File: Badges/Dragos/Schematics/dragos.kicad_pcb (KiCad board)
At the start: 2 copper layers, 78.5 x 67.3 mm, 28 parts, among them J7 USB_C_Receptacle, SW1 SW_DIP_x01, SW2 Prog, SW3 Power, U1 STM32F042F6Px, U2 TLV1117-33, U3 HX4056

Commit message: Progress on Dragos badge
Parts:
- removed BT1: Battery_Cell, Tests:Dongguan14500
- removed C1, C2: 20pF, Capacitor_SMD:C_0805_2012Metric
- removed C10, C11, C6: 1uF, Capacitor_SMD:C_0805_2012Metric
- removed C3, C5: 100nF, Capacitor_SMD:C_0805_2012Metric
- removed C4: 4.7uF, Capacitor_SMD:C_0805_2012Metric
- removed C7: 10nF, Capacitor_SMD:C_0805_2012Metric
- removed C8, C9: 10uF, Capacitor_SMD:C_0805_2012Metric
- removed the G*** at (135.4, 99.1) (x4)
- removed J7: USB_C_Receptacle, Tests:USB_C_Receptical-Jing
- removed R1, R2, R3: 10k, Resistor_SMD:R_0805_2012Metric
- removed R5: 1.5, Resistor_SMD:R_0805_2012Metric
- removed R6: 1k, Resistor_SMD:R_0805_2012Metric
- removed SW1: SW_DIP_x01, Button_Switch_SMD:SW_Push_1P1T_NO_CK_KSC7xxJ
- removed SW2: Prog, BreadBoardPwr:SK-3296S_switch
- removed SW3: Power, BreadBoardPwr:SK-3296S_switch
- removed U1: STM32F042F6Px, Package_SO:TSSOP-20_4.4x6.5mm_P0.65mm
- removed U2: TLV1117-33, Package_TO_SOT_SMD:SOT-223-3_TabPin2
- removed U3: HX4056, Package_SO:HSOP-8-1EP_3.9x4.9mm_P1.27mm_EP2.41x3.1mm
- added G*** (x6): LOGO, LOGO, F.Cu at (0.00, 0.00)
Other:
- board size 78.5 x 67.3 mm -> 98.7 x 84.6 mm

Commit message: Almost done
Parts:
- removed the G*** at (0.00, 0.00) (x6)
- added BT1: Battery_Cell, Tests:Dongguan14500, B.Cu at (134.5, 64.5)
- added C1: 100nF, Capacitor_SMD:C_0805_2012Metric, B.Cu at (271.2, 105.2)
- added C10: 1uF, Capacitor_SMD:C_0805_2012Metric, B.Cu at (127.9, 76.8)
- added C11: 1uF, Capacitor_SMD:C_0805_2012Metric, B.Cu at (142.3, 78.8)
- added C12: 100nF, Capacitor_SMD:C_0805_2012Metric, B.Cu at (239.5, 99.2)
- added C13: 1uF, Capacitor_SMD:C_0805_2012Metric, B.Cu at (280.0, 108.2)
- added C14: 4.7uF, Capacitor_SMD:C_0805_2012Metric, B.Cu at (235.1, 99.2)
- added C15: 10pF, Capacitor_SMD:C_0805_2012Metric, B.Cu at (248.3, 102.1)
- added C16: 10pF, Capacitor_SMD:C_0805_2012Metric, B.Cu at (239.5, 102.1)
- added C17: 2.2pF, Capacitor_SMD:C_0805_2012Metric, B.Cu at (235.1, 102.1)
- added C18: 2.2pF, Capacitor_SMD:C_0805_2012Metric, B.Cu at (243.9, 102.1)
- added C2: 100nF, Capacitor_SMD:C_0805_2012Metric, B.Cu at (275.6, 105.2)
- added C3: 100nF, Capacitor_SMD:C_0805_2012Metric, B.Cu at (280.0, 105.2)
- added C4: 100nF, Capacitor_SMD:C_0805_2012Metric, B.Cu at (271.2, 102.3)
- added C5: 100nF, Capacitor_SMD:C_0805_2012Metric, B.Cu at (275.6, 102.3)
- added C6: 4.7uF, Capacitor_SMD:C_0805_2012Metric, B.Cu at (279.7, 120.0)
- added C7: 100nF, Capacitor_SMD:C_0805_2012Metric, B.Cu at (280.0, 102.3)
- added C8: 10uF, Capacitor_SMD:C_0805_2012Metric, B.Cu at (113.6, 77.7)
- added C9: 10uF, Capacitor_SMD:C_0805_2012Metric, B.Cu at (127.9, 73.5)
- added D1: LED, LED_SMD:LED_0603_1608Metric, B.Cu at (275.2, 99.5)
- added D2: LED, LED_SMD:LED_0603_1608Metric, B.Cu at (279.3, 99.5)
- added D3: LED_ALT, Dragos:T776-ReverseMountLED, B.Cu at (186.5, 80.3)
- added G*** (x2): LOGO, LOGO, F.Cu at (0.00, 0.00)
- added G*** (x4): LOGO, LOGO, F.Cu at (145.3, 95.3)
- added J1: One, Connector_PinHeader_2.54mm:PinHeader_1x08_P2.54mm_Vertical, B.Cu at (230.5, 112.6)
- added J2: Two, Connector_PinHeader_2.54mm:PinHeader_1x11_P2.54mm_Vertical, B.Cu at (208.2, 112.6)
- added J3: CC2530-ISP, Connector_PinHeader_2.54mm:PinHeader_2x05_P2.54mm_Vertical, B.Cu at (235.2, 95.3)
- added J4: Three, Connector_PinHeader_2.54mm:PinHeader_1x14_P2.54mm_Vertical, B.Cu at (203.6, 112.6)
- added J5: Prog, Connector_PinHeader_2.54mm:PinHeader_1x06_P2.54mm_Vertical, B.Cu at (255.2, 112.6)
- added J6: Oled_FFS, Connector_FFC-FPC:TE_1-84953-0_1x10-1MP_P1.0mm_Horizontal, B.Cu at (242.9, 111.1)
- added J7: USB_C_Receptacle, Tests:USB_C_Receptical-Jing, B.Cu at (177.4, 126.2)
- added J8: Four, Connector_PinHeader_2.54mm:PinHeader_1x13_P2.54mm_Vertical, B.Cu at (266.7, 119.1)
- added J9: BreadboardPwr, Connector_PinHeader_2.54mm:PinHeader_1x02_P2.54mm_Vertical, B.Cu at (259.8, 112.6)
- added L1: L_Small, Inductor_SMD:L_0603_1608Metric, B.Cu at (275.2, 97.0)
- added Power ->: Power, BreadBoardPwr:SK-3296S_switch, B.Cu at (162.6, 85.9)
- added R11: 330Ohm, Resistor_SMD:R_0805_2012Metric, B.Cu at (271.2, 111.1)
- added R12: 330Ohm, Resistor_SMD:R_0805_2012Metric, B.Cu at (275.6, 111.1)
- added R13: 4k7, Resistor_SMD:R_0805_2012Metric, B.Cu at (280.0, 111.1)
- added R14: 4k7, Resistor_SMD:R_0805_2012Metric, B.Cu at (271.2, 108.2)
- added R3: 100k, Resistor_SMD:R_0805_2012Metric, B.Cu at (275.6, 108.2)
- added R5: 1.5, Resistor_SMD:R_0805_2012Metric, B.Cu at (113.6, 74.4)
- added R6: 1k, Resistor_SMD:R_0805_2012Metric, B.Cu at (113.7, 80.9)
- added R9: 1k, Resistor_SMD:R_0805_2012Metric, B.Cu at (279.7, 114.1)
- added RN1: 10k, Resistor_SMD:R_Array_Concave_2x0603, B.Cu at (271.1, 99.2)
- added RN2: 4k7, Resistor_SMD:R_Array_Concave_4x0603, B.Cu at (155.8, 109.9)
- added SW1: SW_DIP_x01, Button_Switch_SMD:SW_Push_1P1T_NO_CK_KSC7xxJ, B.Cu at (161.3, 96.7)
- added SW2: SW_DIP_x01, Dragos:1TS002E-2500-2500-CT-HYP-Button, F.Cu at (178.2, 117.9)
- added SW4: SW_DIP_x01, Dragos:1TS002E-2500-2500-CT-HYP-Button, F.Cu at (183.7, 117.9)
- added U1: STM32F411RETx, Package_QFP:LQFP-64_10x10mm_P0.5mm, B.Cu at (163.8, 126.6)
- added U2: TLV1117-33, Package_TO_SOT_SMD:SOT-223-3_TabPin2, B.Cu at (136.3, 76.6)
- added U3: HX4056, Package_SO:HSOP-8-1EP_3.9x4.9mm_P1.27mm_EP2.41x3.1mm, B.Cu at (120.5, 76.3)
- added U4: EByte-CC2530, RF_Module:E18-MS1-PCB, B.Cu at (140.8, 102.8)
- added U5: K1-5202UA-03(5Way_Switch), Dragos:K1-5202UA-03(5way-switch), F.Cu at (151.6, 116.9)
- added Y1: 12MHz, Crystal:Crystal_SMD_SeikoEpson_TSX3225-4Pin_3.2x2.5mm, B.Cu at (260.1, 105.5)
- added Y2: 32.768kHz, Crystal:Crystal_SMD_3215-2Pin_3.2x1.5mm, B.Cu at (222.1, 77.5)
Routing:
- net Net-(C11-Pad1): track 0.00 -> 51.9 mm
- net VDDA: track 0.00 -> 35.2 mm

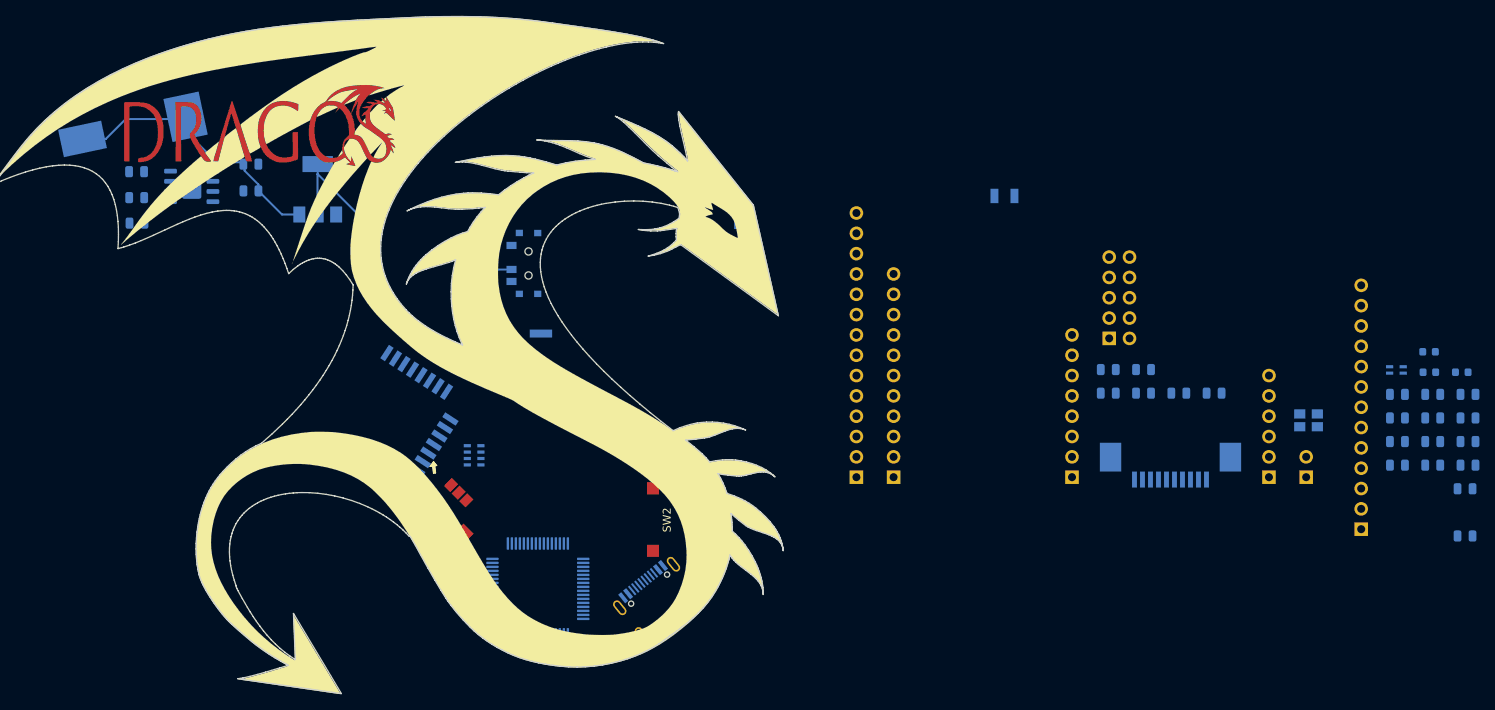
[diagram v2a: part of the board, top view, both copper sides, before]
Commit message: Added bom
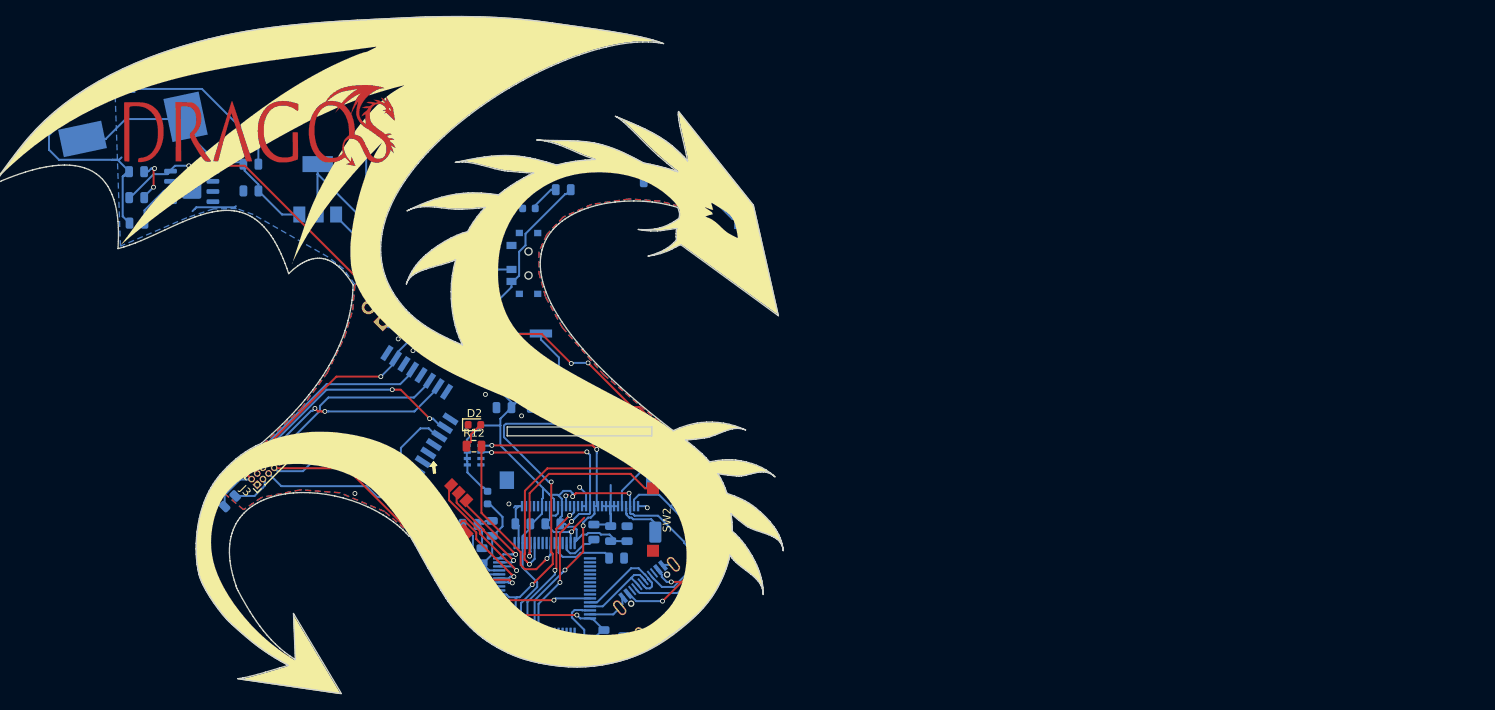
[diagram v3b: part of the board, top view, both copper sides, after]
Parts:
- removed the G*** at (0.00, 0.00) (x2)
- removed the G*** at (145.3, 95.3) (x4)
- removed J1: One, Connector_PinHeader_2.54mm:PinHeader_1x08_P2.54mm_Vertical
- removed J2: Two, Connector_PinHeader_2.54mm:PinHeader_1x11_P2.54mm_Vertical
- removed J4: Three, Connector_PinHeader_2.54mm:PinHeader_1x14_P2.54mm_Vertical
- removed J6: Oled_FFS, Connector_FFC-FPC:TE_1-84953-0_1x10-1MP_P1.0mm_Horizontal
- removed J8: Four, Connector_PinHeader_2.54mm:PinHeader_1x13_P2.54mm_Vertical
- added C19: 100nF, Capacitor_SMD:C_0805_2012Metric, B.Cu at (159.5, 103.9)
- added C20: 4.7uF, Capacitor_SMD:C_0805_2012Metric, B.Cu at (163.8, 103.9)
- added C21: 4.7uF, Capacitor_SMD:C_2010_5025Metric_Pad1.52x2.65mm_HandSolder, B.Cu at (180.8, 119.5)
- added C22: 100nF, Capacitor_SMD:C_0805_2012Metric, B.Cu at (183.6, 112.2)
- added C23: 10uF, Capacitor_SMD:C_0805_2012Metric, B.Cu at (183.6, 116.1)
- added G*** (x2): LOGO, LOGO, F.Cu at (0.00, 0.00)
- added G*** (x4): LOGO, LOGO, F.Cu at (145.3, 95.3)
- added R1: 760k, Resistor_SMD:R_0805_2012Metric, B.Cu at (180.7, 109.6)
- added U6: Formike-OLED, Connector_FFC-FPC:Hirose_FH12-30S-0.5SH_1x30-1MP_P0.50mm_Horizontal, B.Cu at (169.1, 114.4)
- D2, R12: moved to F.Cu
- J3: footprint Connector_PinHeader_2.54mm:PinHeader_2x05_P2.54mm_Vertical -> Connector_PinHeader_1.00mm:PinHeader_2x05_P1.00mm_Vertical; moved to F.Cu
- J5: footprint Connector_PinHeader_2.54mm:PinHeader_1x06_P2.54mm_Vertical -> Connector_PinHeader_1.00mm:PinHeader_1x06_P1.00mm_Vertical; moved to F.Cu
- Power->1: renamed from Power ->; value Power -> SW3
- moved R9 154.4 mm to (125.3, 115.6), turned to 225 degrees
- moved C13 124.1 mm to (156.8, 122.4), turned to 90 degrees
- moved D2 123.6 mm to (155.9, 106.1)
- moved R12 119.9 mm to (155.8, 108.8)
- moved L1 119.1 mm to (157.5, 115.2), turned to 90 degrees
- moved J9 117.0 mm to (144.4, 93.2), turned to 45 degrees
- moved C2 116.4 mm to (163.1, 134.7)
- moved D1 114.4 mm to (162.7, 79.0)
- moved C7 111.9 mm to (168.2, 103.8), turned to 180 degrees
- moved C1 110.1 mm to (161.9, 118.5), turned to 180 degrees
- moved R11 109.8 mm to (167.0, 76.7)
- moved J3 108.1 mm to (128.7, 113.6), turned to 135 degrees
- moved C5 108.0 mm to (172.0, 132.7), turned to 270 degrees
- moved Y1 107.9 mm to (153.5, 122.4)
- moved R13 107.1 mm to (173.6, 122.7)
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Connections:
- R12 pad 2: PA3 -> PB0
- U5 pad 4: PA3 -> PC3
- U5 pad 6: PA4 -> PC2
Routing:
- net VCC: track 0.00 -> 210.2 mm, vias 0 -> 6
- net VSS: track 0.00 -> 207.9 mm, vias 0 -> 23
- net +5V: track 0.00 -> 119.4 mm, vias 0 -> 5
- net RST: track 0.00 -> 65.1 mm, vias 0 -> 4
- net PA10: track 0.00 -> 54.1 mm, vias 0 -> 1
- net PB7: track 0.00 -> 41.1 mm, vias 0 -> 4
- net PB6: track 0.00 -> 39.1 mm, vias 0 -> 4
- net PA6: track 0.00 -> 36.1 mm, vias 0 -> 1
- net Net-(J3-Pad6): track 0.00 -> 29.9 mm, vias 0 -> 2
- net Net-(J3-Pad5): track 0.00 -> 28.5 mm
- net Net-(J3-Pad4): track 0.00 -> 26.7 mm
- net PA5: track 0.00 -> 26.5 mm, vias 0 -> 1
- net Net-(J3-Pad8): track 0.00 -> 26.3 mm, vias 0 -> 2
- net Net-(C21-Pad2): track 0.00 -> 23.9 mm
- net Net-(J3-Pad10): track 0.00 -> 23.3 mm
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- added copper zone on B.Cu, net VSS
- added copper zone on F.Cu, net VSS
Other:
- outline, holes or cut-outs redrawn
